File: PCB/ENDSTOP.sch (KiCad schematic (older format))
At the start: 4 parts, among them J9 ENDSTOP_CONN, SW3 ENDSTOP

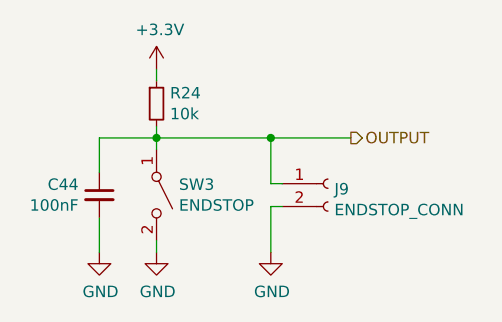
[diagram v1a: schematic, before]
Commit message: Increased VCC from 3v3 to 5v
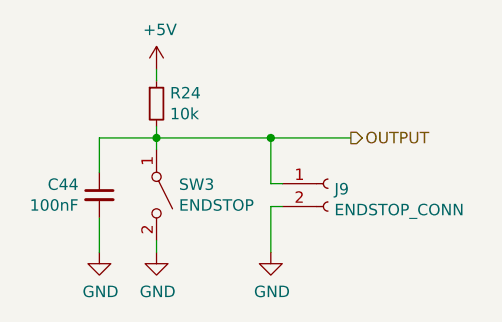
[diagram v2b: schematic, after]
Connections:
- net +3V3 renamed +5V
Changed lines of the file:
@@
 $Descr A4 11693 8268
 encoding utf-8
-Sheet 16 25
+Sheet 17 25
 Title ""
 Date ""
@@
 Wire Wire Line
 	5900 4400 5900 4250
-$Comp
-L power:+3.3V #PWR0123
-U 1 1 5E8AA8C2
-P 6150 3600
-F 0 "#PWR0123" H 6150 3450 50  0001 C CNN
-F 1 "+3.3V" H 6165 3773 50  0000 C CNN
-F 2 "" H 6150 3600 50  0001 C CNN
-F 3 "" H 6150 3600 50  0001 C CNN
-	1    6150 3600
-	1    0    0    -1
-$EndComp
 Wire Wire Line
 	6150 3600 6150 3650
@@
 Wire Wire Line
 	6650 4200 6700 4200
+$Comp
+L power:+5V #PWR?
+U 1 1 5E90B50E
+P 6150 3600
+F 0 "#PWR?" H 6150 3450 50  0001 C CNN
+F 1 "+5V" H 6165 3773 50  0000 C CNN
+F 2 "" H 6150 3600 50  0001 C CNN
+F 3 "" H 6150 3600 50  0001 C CNN
+	1    6150 3600
+	1    0    0    -1
+$EndComp
 $EndSCHEMATC

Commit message: Added Humidity and temperature sensors
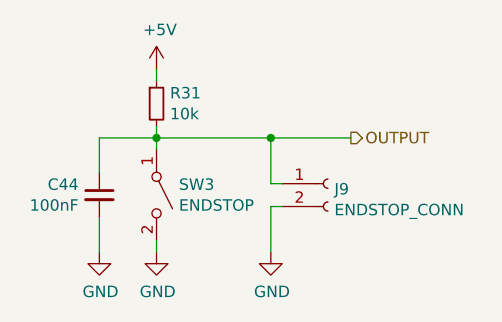
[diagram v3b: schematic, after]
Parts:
- renumbered R24 to R31
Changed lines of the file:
@@
 $EndComp
 $Comp
-L Device:R_Small R24
+L Device:R_Small R31
 U 1 1 5E8A974E
 P 6150 3750
-F 0 "R24" H 6209 3796 50  0000 L CNN
+F 0 "R31" H 6209 3796 50  0000 L CNN
 F 1 "10k" H 6209 3705 50  0000 L CNN
 F 2 "" H 6150 3750 50  0001 C CNN
@@
 	6150 3900 6150 3950
 $Comp
-L power:GND #PWR0122
+L power:GND #PWR0125
 U 1 1 5E8A9B1B
 P 5900 4400
-F 0 "#PWR0122" H 5900 4150 50  0001 C CNN
+F 0 "#PWR0125" H 5900 4150 50  0001 C CNN
 F 1 "GND" H 5905 4227 50  0000 C CNN
 F 2 "" H 5900 4400 50  0001 C CNN
@@
 $EndComp
 $Comp
-L power:GND #PWR0124
+L power:GND #PWR0127
 U 1 1 5E8A9B96
 P 6150 4400
-F 0 "#PWR0124" H 6150 4150 50  0001 C CNN
+F 0 "#PWR0127" H 6150 4150 50  0001 C CNN
 F 1 "GND" H 6155 4227 50  0000 C CNN
 F 2 "" H 6150 4400 50  0001 C CNN
@@
 	6650 3900 6150 3900
 $Comp
-L power:GND #PWR0125
+L power:GND #PWR0128
 U 1 1 5E8AD764
 P 6650 4400
-F 0 "#PWR0125" H 6650 4150 50  0001 C CNN
+F 0 "#PWR0128" H 6650 4150 50  0001 C CNN
 F 1 "GND" H 6655 4227 50  0000 C CNN
 F 2 "" H 6650 4400 50  0001 C CNN
@@
 U 1 1 5E90B50E
 P 6150 3600
-F 0 "#PWR?" H 6150 3450 50  0001 C CNN
+AR Path="/5E8A6686/5E90B50E" Ref="#PWR?"  Part="1"
+AR Path="/5E89F314/5E90B50E" Ref="#PWR0126"  Part="1"
+F 0 "#PWR0126" H 6150 3450 50  0001 C CNN
 F 1 "+5V" H 6165 3773 50  0000 C CNN
 F 2 "" H 6150 3600 50  0001 C CNN
